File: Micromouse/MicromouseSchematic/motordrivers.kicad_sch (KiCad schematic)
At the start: 11 parts, among them J1 Conn_01x06_MountingPin, J2 Conn_01x06_MountingPin, U11 MP6550GG-Z, U7 MP6550GG-Z

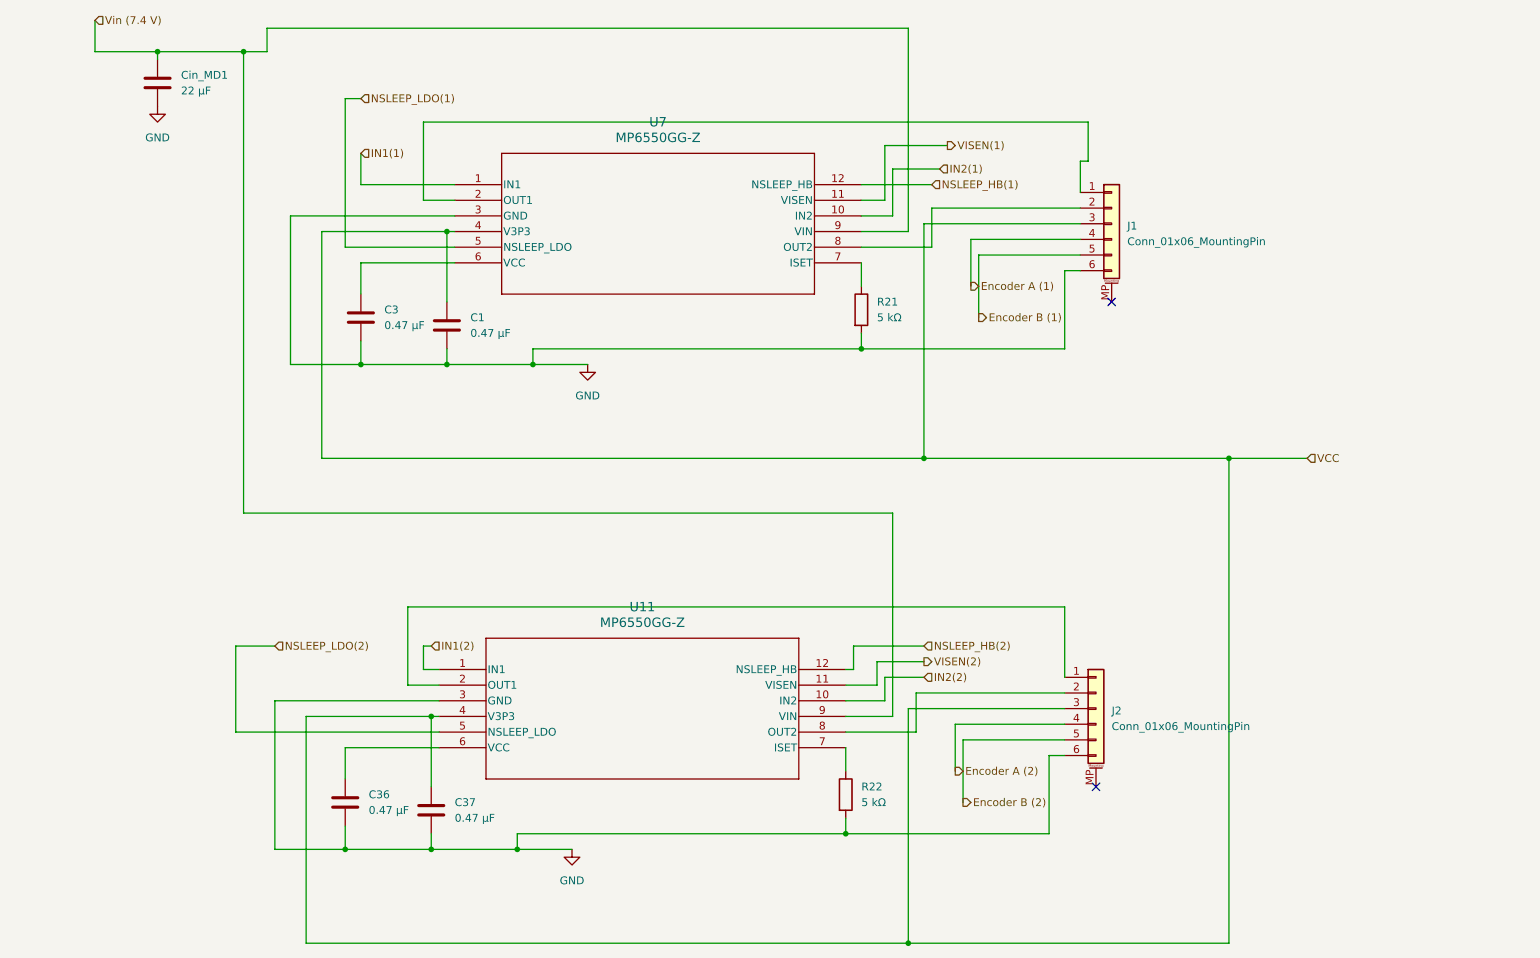
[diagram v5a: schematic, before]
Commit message: Micromouse KiCad: STM32-centric routing; ERC errors 23→6; backups and gitignore
Body:
Connected almost all STM32 signals; ERC down to 6

Rework root schematic plus motor driver, IMU/magnetometer, IR sensor, and TOF
subsheets so the bulk of signals reach the STM32. KiCad ERC is not fully clean
yet, but major nets are in place: errors dropped from 23 to 6 while many
previously unconnected signals were wired.

Add 2026-04-08 schematic backup zips. Extend .gitignore for macOS .DS_Store
paths. Update MicromouseSchematic.kicad_prl.
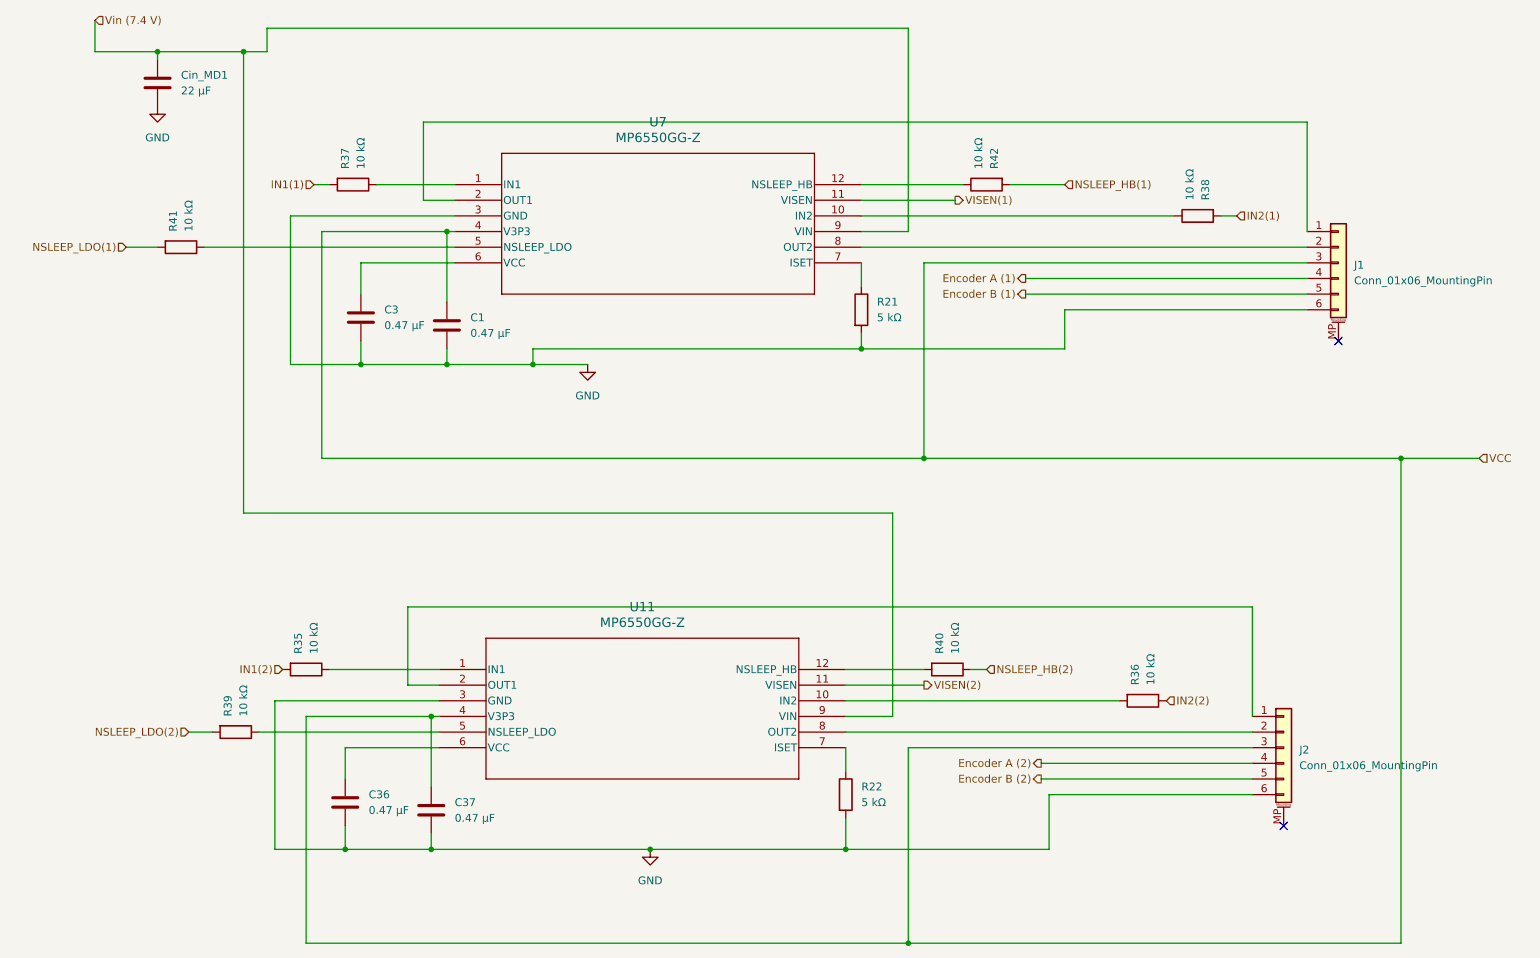
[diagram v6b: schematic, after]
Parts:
- added R35, R36, R37, R38, R39, R40, R41, R42: 10 kΩ, symbol Device:R
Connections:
- net IN1(1): now also R37.2; no longer U7.1 (IN1)
- net IN1(2): now also R35.2; no longer U11.1 (IN1)
- net IN2(1): now also R38.2; no longer U7.10 (IN2)
- net IN2(2): now also R36.1; no longer U11.10 (IN2)
- net NSLEEP_HB(1): now also R42.2; no longer U7.12 (NSLEEP_HB)
- net NSLEEP_HB(2): now also R40.1; no longer U11.12 (NSLEEP_HB)
- net NSLEEP_LDO(1): now also R41.2; no longer U7.5 (NSLEEP_LDO)
- net NSLEEP_LDO(2): now also R39.2; no longer U11.5 (NSLEEP_LDO)
- new net: R41.1, U7.5 (NSLEEP_LDO)
- new net: R35.1, U11.1 (IN1)
- new net: R39.1, U11.5 (NSLEEP_LDO)
- new net: R40.2, U11.12 (NSLEEP_HB)
- new net: R42.1, U7.12 (NSLEEP_HB)
- new net: R38.1, U7.10 (IN2)
- new net: R36.2, U11.10 (IN2)
- new net: R37.1, U7.1 (IN1)
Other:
- moved on the sheet: J1, J2

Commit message: Micromouse KiCad: MP6550 layout, schematic updates; ERC clean, warnings ~5–6
Relocate MP6550G-Z symbol and footprint trees from MicromouseSchematic into
Micromouse/MP6550G-Z and refresh sym-lib-table (portable ${KIPRJMOD} paths
where applicable, MP6550 at new location).

Update root schematic plus IMU, IR, motor driver, and TOF subsheets. KiCad
ERC: all errors resolved (previously 6 remaining after earlier bring-up).
Warnings reduced from roughly 35–40+ down to about 5–6.

Add MicromouseSchematic-2026-04-11_212024.zip backup.
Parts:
- U11, U7: footprint MM_MP6550G-Z:MP6550_MNP -> Library:IC12_MP6550_MNP
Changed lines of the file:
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@@
 			)
 		)
-		(property "Footprint" "MM_MP6550G-Z:MP6550_MNP"
+		(property "Footprint" "Library:IC12_MP6550_MNP"
 			(at 80.01 128.27 0)
 			(effects
@@
 			)
 		)
-		(property "Footprint" "MM_MP6550G-Z:MP6550_MNP"
+		(property "Footprint" "Library:IC12_MP6550_MNP"
 			(at 82.55 49.53 0)
 			(effects

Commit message: fix: footprint errors and add setup guide
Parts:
- U11, U7: footprint Library:IC12_MP6550_MNP -> MM_MP6550G-Z:MP6550_MNP
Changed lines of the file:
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@@
 			)
 		)
-		(property "Footprint" "Library:IC12_MP6550_MNP"
+		(property "Footprint" "MM_MP6550G-Z:MP6550_MNP"
 			(at 80.01 128.27 0)
 			(effects
@@
 			)
 		)
-		(property "Footprint" "Library:IC12_MP6550_MNP"
+		(property "Footprint" "MM_MP6550G-Z:MP6550_MNP"
 			(at 82.55 49.53 0)
 			(effects
